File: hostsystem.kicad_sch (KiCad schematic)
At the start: 36 parts, among them J1001 TC2050, J1002 Conn_01x03_Pin, U1001 AM6231ASGGGAALW, U1002 SN74LVC2G241DCUR, U1003 AT24C32D-STUM-T, X1001 32.768kHz, X1002 25MHz

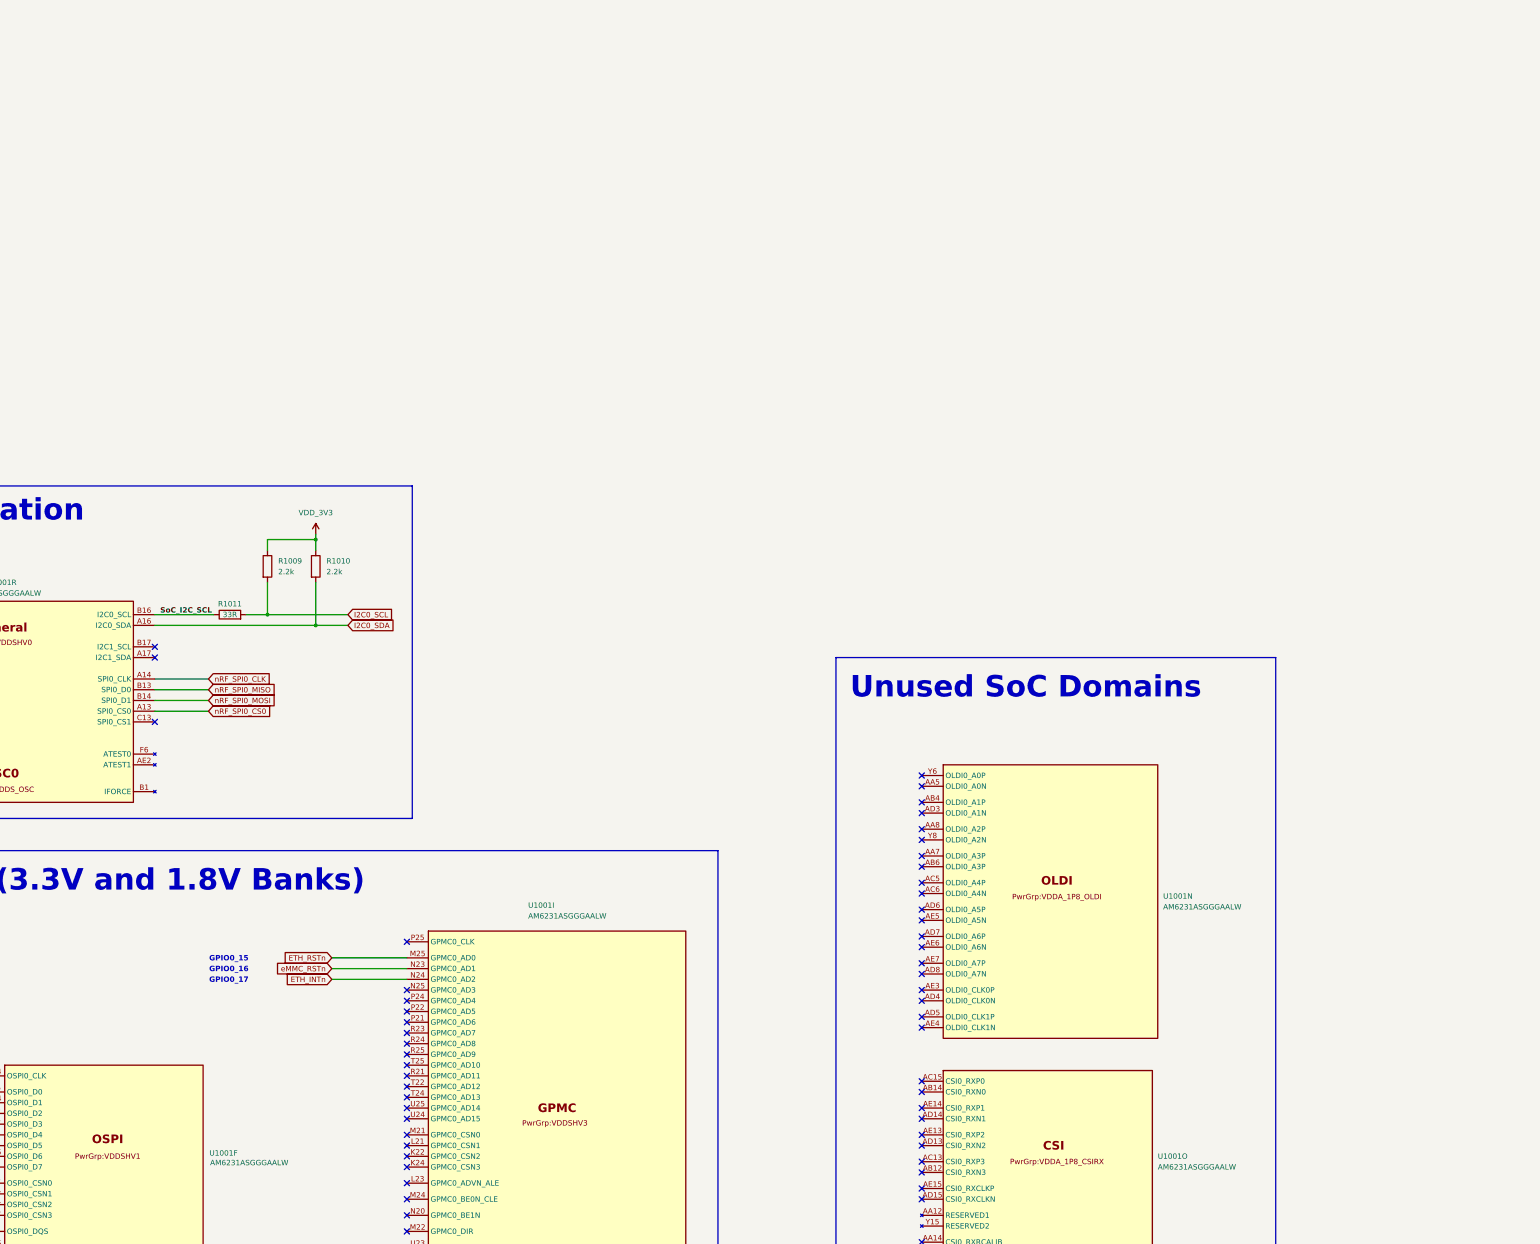
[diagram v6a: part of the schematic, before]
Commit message: Double checked power, ddr4, USB, MMC and added bootstrap. Also added buttons and added pinmuxing in sysconfig
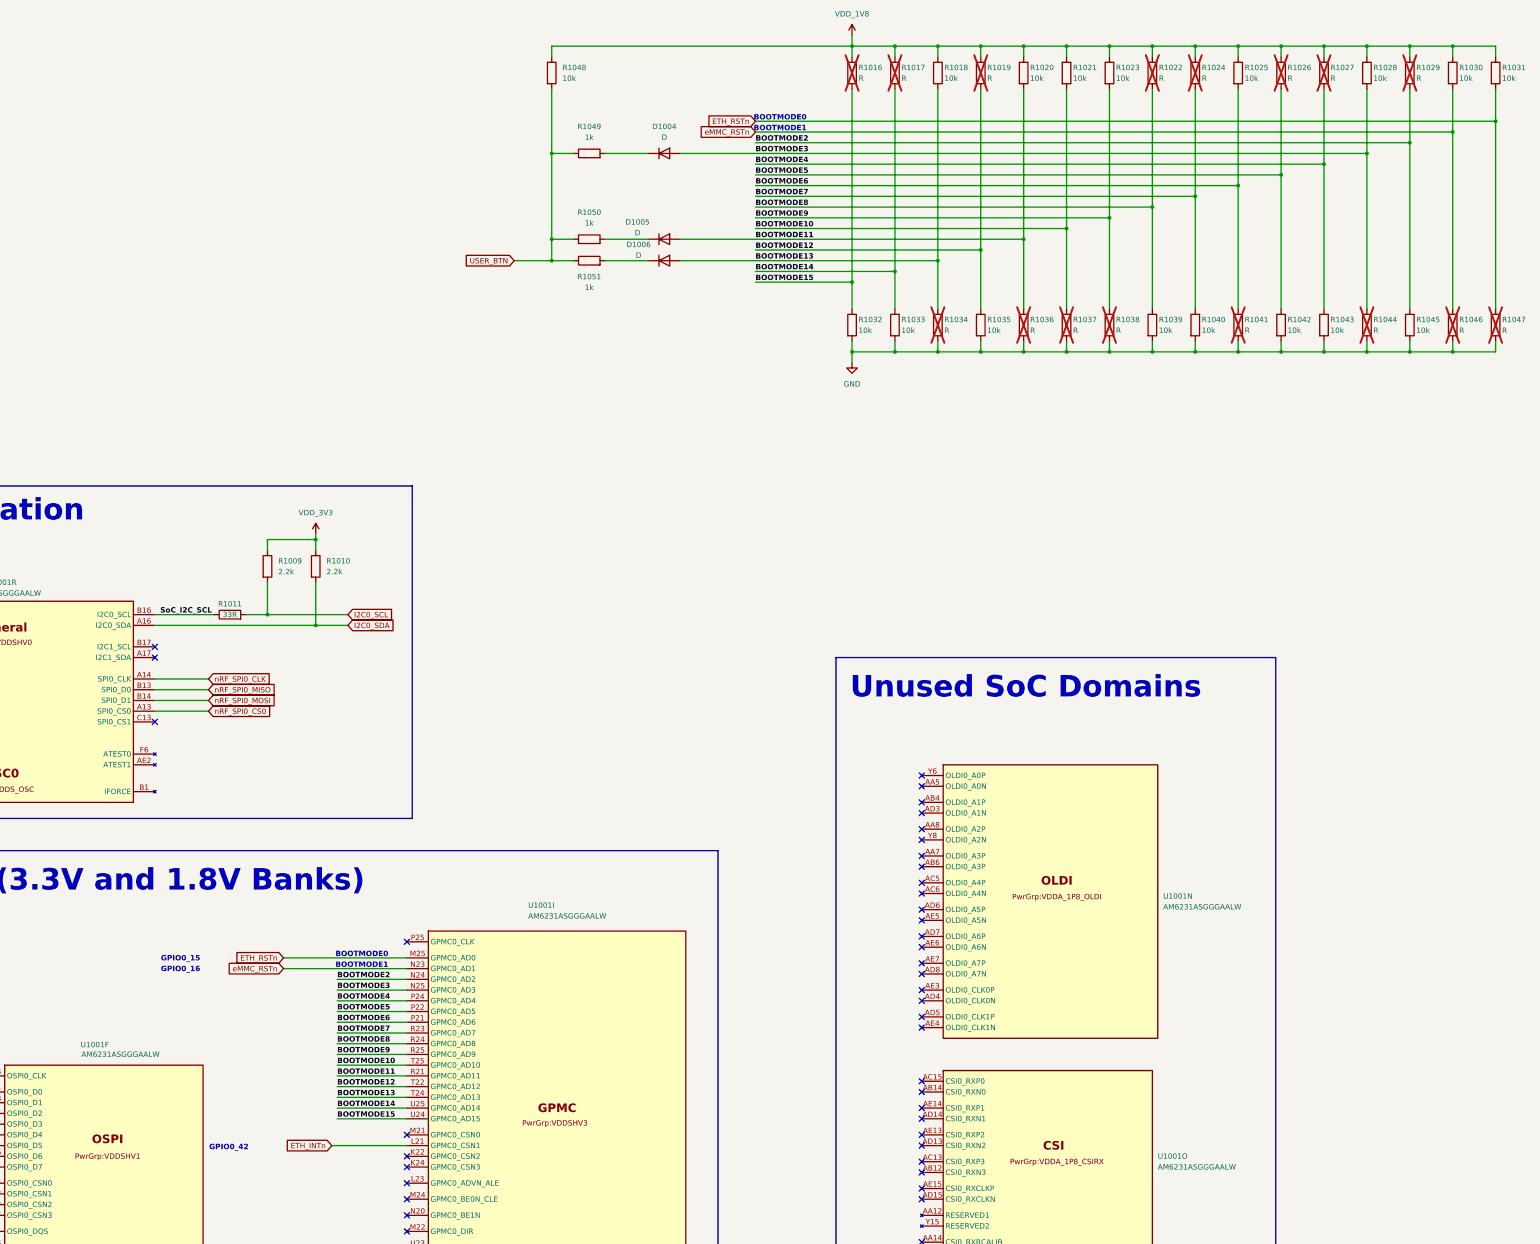
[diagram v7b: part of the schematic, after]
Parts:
- added D1004, D1005, D1006: D, symbol Device:D
- added R1016, R1017, R1019, R1022, R1024, R1026, R1027, R1029, R1034, R1036, R1037, R1038, R1041, R1044, R1046, R1047: R, symbol Device:R
- added R1018, R1020, R1021, R1023, R1025, R1028, R1030, R1031, R1032, R1033, R1035, R1039, R1040, R1042, R1043, R1045, R1048: 10k, symbol Device:R
- added R1049, R1050, R1051: 1k, symbol Device:R
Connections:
- net ETH_INTn: now also U1001.L21 (GPMC0_CSN1); no longer U1001.N24 (GPMC0_AD2)
- net ETH_RSTn: now also R1031.2, R1047.1
- net GND: now also R1032.2, R1033.2, R1034.2, R1035.2, R1036.2, R1037.2, R1038.2, R1039.2, R1040.2, R1041.2, R1042.2, R1043.2, R1044.2, R1045.2, R1046.2, R1047.2
- net VDD_1V8: now also R1016.1, R1017.1, R1018.1, R1019.1, R1020.1, R1021.1, R1022.1, R1023.1, R1024.1, R1025.1, R1026.1, R1027.1, R1028.1, R1029.1, R1030.1, R1031.1, R1048.1
- net eMMC_RSTn: now also R1030.2, R1046.1
- net BOOTMODE3: now reaches U1001.N25 (GPMC0_AD3)
- net BOOTMODE3: now also D1004.2 (A), R1028.2, R1044.1
- net BOOTMODE6: now reaches U1001.P21 (GPMC0_AD6)
- net BOOTMODE6: now also R1025.2, R1041.1
- net BOOTMODE5: now reaches U1001.P22 (GPMC0_AD5)
- net BOOTMODE5: now also R1026.2, R1042.1
- net BOOTMODE4: now reaches U1001.P24 (GPMC0_AD4)
- net BOOTMODE4: now also R1027.2, R1043.1
- net BOOTMODE11: now reaches U1001.R21 (GPMC0_AD11)
- net BOOTMODE11: now also D1005.2 (A), R1020.2, R1036.1
- net BOOTMODE7: now reaches U1001.R23 (GPMC0_AD7)
- net BOOTMODE7: now also R1024.2, R1040.1
- net BOOTMODE8: now reaches U1001.R24 (GPMC0_AD8)
- net BOOTMODE8: now also R1022.2, R1039.1
- net BOOTMODE9: now reaches U1001.R25 (GPMC0_AD9)
- net BOOTMODE9: now also R1023.2, R1038.1
- net BOOTMODE12: now reaches U1001.T22 (GPMC0_AD12)
- net BOOTMODE12: now also R1019.2, R1035.1
- net BOOTMODE13: now reaches U1001.T24 (GPMC0_AD13)
- net BOOTMODE13: now also D1006.2 (A), R1018.2, R1034.1
- net BOOTMODE10: now reaches U1001.T25 (GPMC0_AD10)
- net BOOTMODE10: now also R1021.2, R1037.1
- net BOOTMODE15: now reaches U1001.U24 (GPMC0_AD15)
- net BOOTMODE15: now also R1016.2, R1032.1
- net BOOTMODE14: now reaches U1001.U25 (GPMC0_AD14)
- net BOOTMODE14: now also R1017.2, R1033.1
- new net: D1004.1 (K), R1049.2
- new net: D1006.1 (K), R1051.2
- new net: D1005.1 (K), R1050.2
- new net BOOTMODE2: R1029.2, R1045.1, U1001.N24 (GPMC0_AD2)
- new net USER_BTN: R1048.2, R1049.1, R1050.1, R1051.1
- no-connect marks 123 -> 109
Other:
- note added: "BOOTMODE0"
- note added: "BOOTMODE1"
- note added: "GPIO0_42"
- note removed: "GPIO0_17"

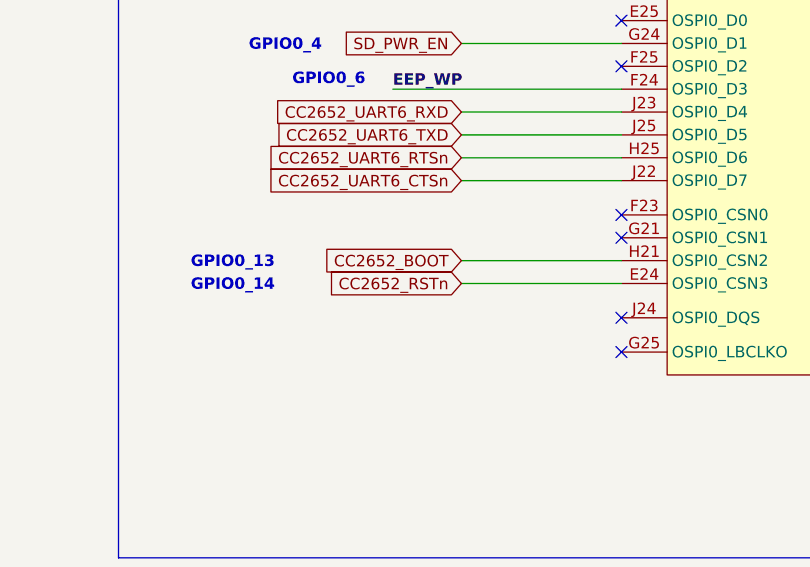
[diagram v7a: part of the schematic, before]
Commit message: Added header pins for UART5
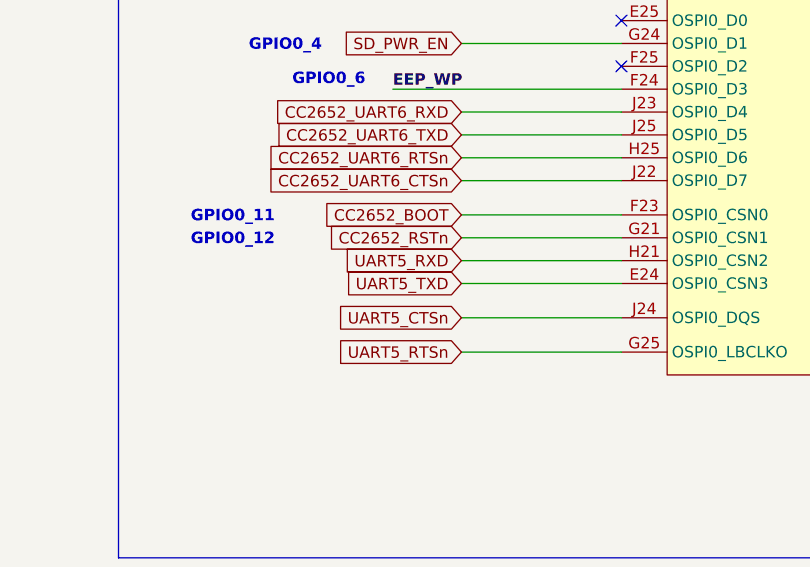
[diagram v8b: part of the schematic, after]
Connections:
- net CC2652_BOOT: now also U1001.F23 (OSPI0_CSN0); no longer U1001.H21 (OSPI0_CSN2)
- net CC2652_RSTn: now also U1001.G21 (OSPI0_CSN1); no longer U1001.E24 (OSPI0_CSN3)
- net UART5_RTSn: now reaches U1001.G25 (OSPI0_LBCLKO)
- net UART5_CTSn: now reaches U1001.J24 (OSPI0_DQS)
- new net UART5_RXD: U1001.H21 (OSPI0_CSN2)
- new net UART5_TXD: U1001.E24 (OSPI0_CSN3)
- no-connect marks 109 -> 105
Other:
- note added: "GPIO0_11"
- note added: "GPIO0_12"
- note removed: "GPIO0_13"
- note removed: "GPIO0_14"
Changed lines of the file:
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@@
 		)
 	)
-	(text "GPIO0_14"
+	(text "GPIO0_12"
 		(exclude_from_sim no)
-		(at 279.4 320.294 0)
+		(at 279.4 315.214 0)
 		(effects
 			(font
@@
 		)
 	)
-	(text "GPIO0_13"
+	(text "GPIO0_11"
 		(exclude_from_sim no)
-		(at 279.4 317.754 0)
+		(at 279.4 312.674 0)
 		(effects
 			(font
@@
 	)
 	(no_connect
-		(at 322.58 312.42)
-	)
-	(no_connect
 		(at 119.38 288.29)
 	)
@@
 	)
 	(no_connect
-		(at 322.58 323.85)
-	)
-	(no_connect
 		(at 544.83 300.99)
 	)
 	(no_connect
-		(at 322.58 327.66)
-	)
-	(no_connect
 		(at 543.56 383.54)
 	)
@@
 	)
 	(no_connect
-		(at 322.58 314.96)
-	)
-	(no_connect
 		(at 544.83 356.87)
 	)
@@
 	(wire
 		(pts
-			(xy 304.8 317.5) (xy 322.58 317.5)
+			(xy 304.8 312.42) (xy 322.58 312.42)
 		)
 		(stroke
@@
 	(wire
 		(pts
+			(xy 304.8 323.85) (xy 322.58 323.85)
+		)
+		(stroke
+			(width 0)
+			(type default)
+		)
+	)
+	(wire
+		(pts
 			(xy 185.42 189.23) (xy 196.85 189.23)
 		)
@@
 	(wire
 		(pts
+			(xy 304.8 320.04) (xy 322.58 320.04)
+		)
+		(stroke
+			(width 0)
+			(type default)
+		)
+	)
+	(wire
+		(pts
 			(xy 660.4 115.57) (xy 660.4 113.03)
 		)
@@
 	(wire
 		(pts
-			(xy 304.8 320.04) (xy 322.58 320.04)
+			(xy 304.8 314.96) (xy 322.58 314.96)
 		)
 		(stroke
@@
 	(wire
 		(pts
+			(xy 304.8 317.5) (xy 322.58 317.5)
+		)
+		(stroke
+			(width 0)
+			(type default)
+		)
+	)
+	(wire
+		(pts
 			(xy 389.89 160.02) (xy 389.89 162.56)
 		)
@@
 	(wire
 		(pts
+			(xy 304.8 327.66) (xy 322.58 327.66)
+		)
+		(stroke
+			(width 0)
+			(type default)
+		)
+	)
+	(wire
+		(pts
 			(xy 459.74 391.16) (xy 459.74 393.7)
 		)
@@
 	(global_label "CC2652_BOOT"
 		(shape input)
-		(at 304.8 317.5 180)
+		(at 304.8 312.42 180)
 		(fields_autoplaced yes)
 		(effects
@@
 		)
 		(property "Intersheetrefs" "${INTERSHEET_REFS}"
-			(at 288.5706 317.5 0)
+			(at 288.5706 312.42 0)
 			(effects
 				(font
@@
 		)
 	)
+	(global_label "UART5_TXD"
+		(shape input)
+		(at 304.8 320.04 180)
+		(fields_autoplaced yes)
+		(effects
+			(font
+				(size 1.27 1.27)
+			)
+			(justify right)
+		)
+		(property "Intersheetrefs" "${INTERSHEET_REFS}"
+			(at 291.5339 320.04 0)
+			(effects
+				(font
+					(size 1.27 1.27)
+				)
+				(justify right)
+				(hide yes)
+			)
+		)
+	)
+	(global_label "UART5_RTSn"
+		(shape input)
+		(at 304.8 327.66 180)
+		(fields_autoplaced yes)
+		(effects
+			(font
+				(size 1.27 1.27)
+			)
+			(justify right)
+		)
+		(property "Intersheetrefs" "${INTERSHEET_REFS}"
+			(at 290.3849 327.66 0)
+			(effects
+				(font
+					(size 1.27 1.27)
+				)
+				(justify right)
+				(hide yes)
+			)
+		)
+	)
 	(global_label "I2C0_SDA"
 		(shape input)
@@
 		)
 	)
+	(global_label "UART5_RXD"
+		(shape input)
+		(at 304.8 317.5 180)
+		(fields_autoplaced yes)
+		(effects
+			(font
+				(size 1.27 1.27)
+			)
+			(justify right)
+		)
+		(property "Intersheetrefs" "${INTERSHEET_REFS}"
+			(at 291.2315 317.5 0)
+			(effects
+				(font
+					(size 1.27 1.27)
+				)
+				(justify right)
+				(hide yes)
+			)
+		)
+	)
 	(global_label "ETH_MDC"
 		(shape input)
@@
 		)
 	)
+	(global_label "UART5_CTSn"
+		(shape input)
+		(at 304.8 323.85 180)
+		(fields_autoplaced yes)
+		(effects
+			(font
+				(size 1.27 1.27)
+			)
+			(justify right)
+		)
+		(property "Intersheetrefs" "${INTERSHEET_REFS}"
+			(at 290.3849 323.85 0)
+			(effects
+				(font
+					(size 1.27 1.27)
+				)
+				(justify right)
+				(hide yes)
+			)
+		)
+	)
 	(global_label "MCU_PORz"
 		(shape input)
@@
 	(global_label "CC2652_RSTn"
 		(shape input)
-		(at 304.8 320.04 180)
+		(at 304.8 314.96 180)
 		(fields_autoplaced yes)
 		(effects
@@
 		)
 		(property "Intersheetrefs" "${INTERSHEET_REFS}"
-			(at 288.8731 320.04 0)
+			(at 288.8731 314.96 0)
 			(effects
 				(font
